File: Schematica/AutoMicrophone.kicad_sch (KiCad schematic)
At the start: 17 parts, among them J1 XLR3_Ground, J2 XLR3_Ground, J3 Jack-DC, Q1 IRLZ44N, Q2 IRLZ44N, Q3 2N3904, U1 SPX2920U-5.0_TO220, U2 ATtiny85-20P

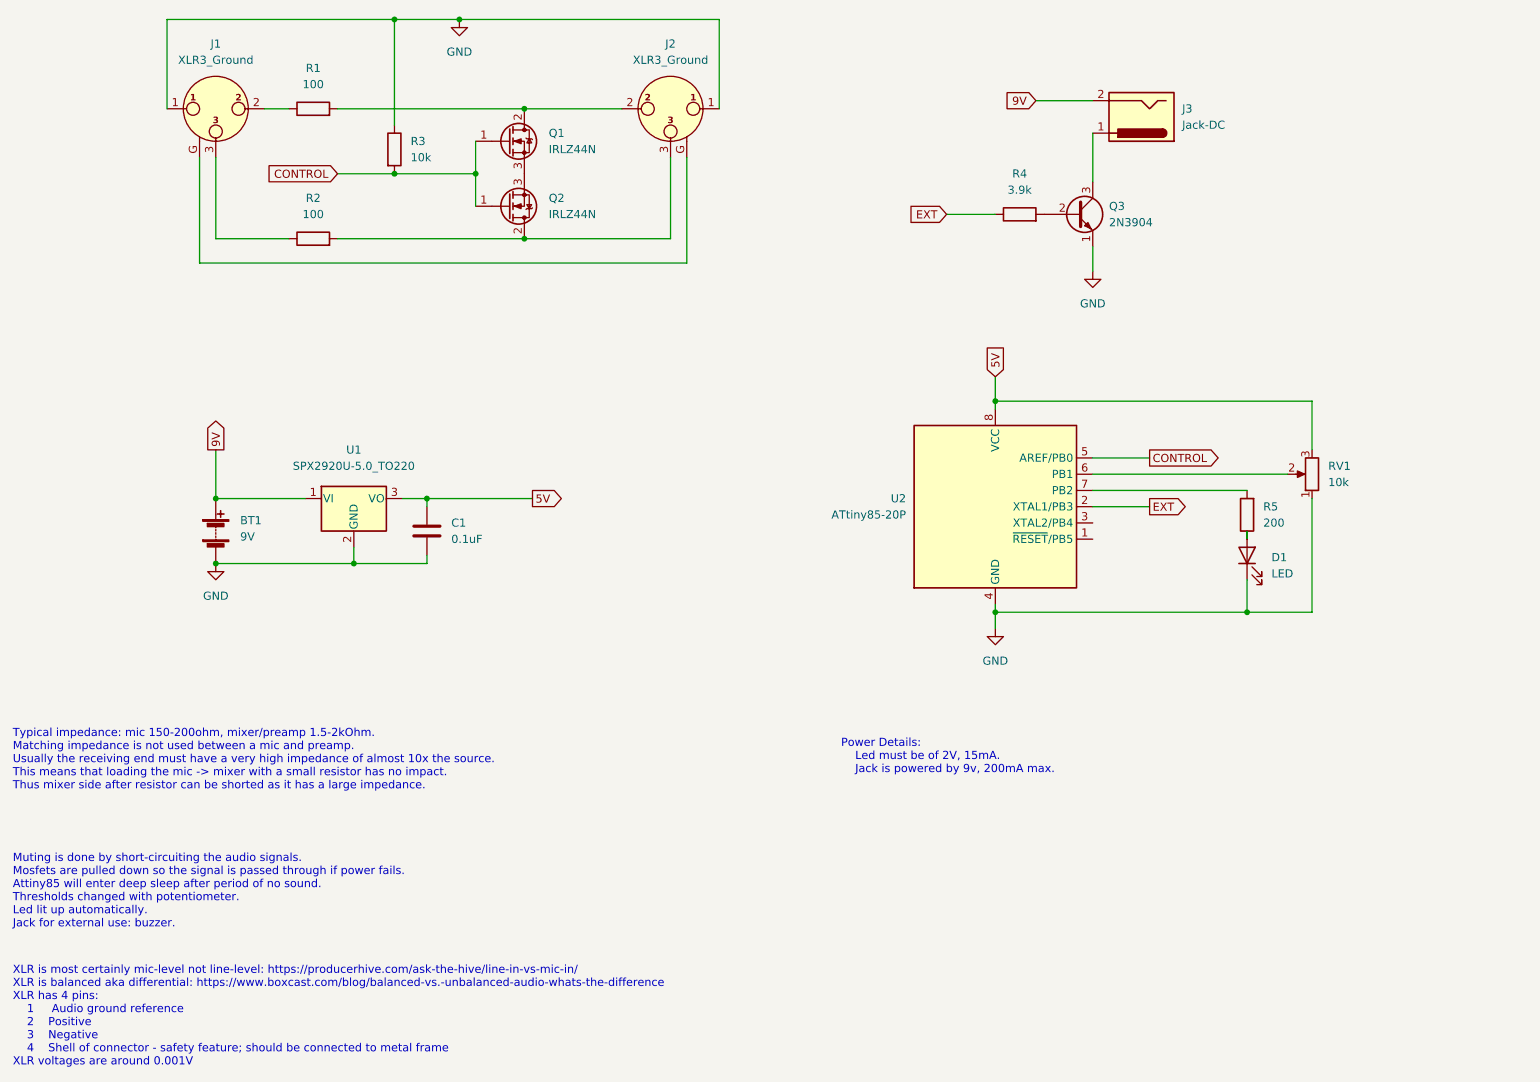
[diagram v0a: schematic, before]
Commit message: Added opamp circuit
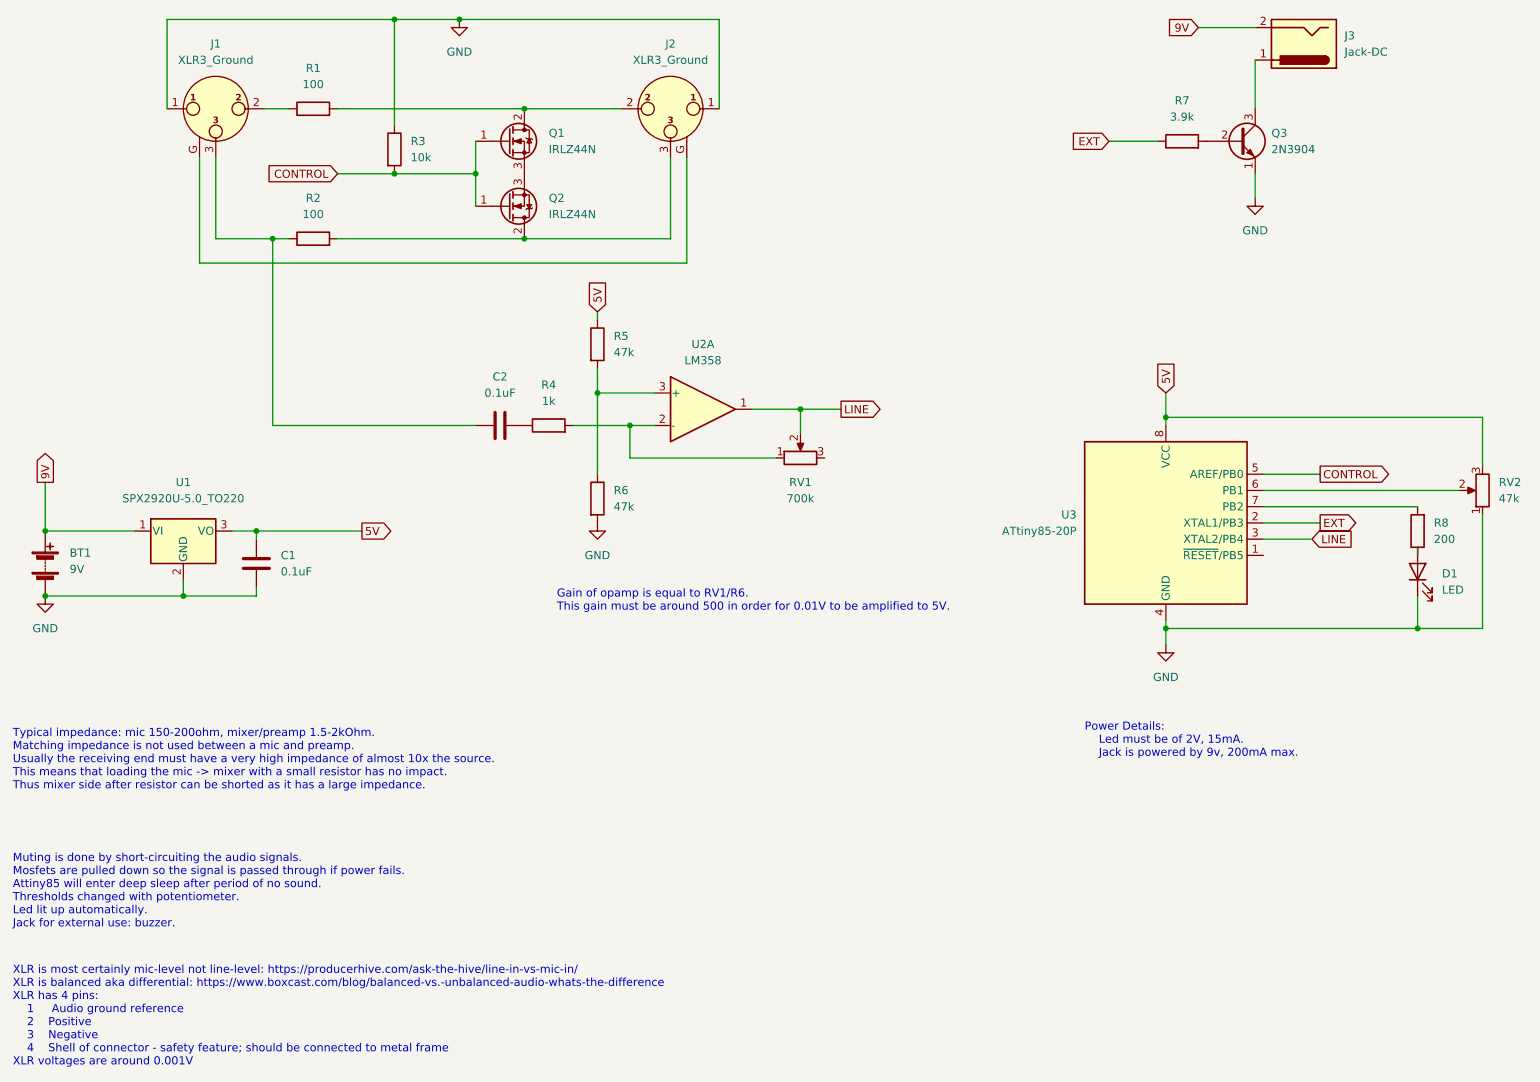
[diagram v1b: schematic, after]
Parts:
- added C2: 0.1uF, symbol Device:C
- added R4: 1k, symbol Device:R
- added R5, R6: 47k, symbol Device:R
- added RV1: 700k, symbol Device:R_Potentiometer
- added U2: LM358, symbol Amplifier_Operational:LM358
- RV2: renamed from RV1; value 10k -> 47k
- renumbered R4 to R7, R5 to R8, U2 to U3
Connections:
- net 5V: now also R5.1
- net GND: now also R6.2
- net at J1.3, R2.1: now also C2.2
- net LINE: now reaches U3.3 (XTAL2/PB4)
- net LINE: now also RV1.2, U2.1
- new net: R4.2, RV1.1, U2.2 (-)
- new net: C2.1, R4.1
- new net: R5.2, R6.1, U2.3 (+)
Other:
- note added: "Gain of opamp is equal to RV1/R6. This gain must be around 500 in order for 0.01V to be amplified to 5V."
- moved on the sheet: BT1, C1, D1, J3, Q3, R7, R8, RV2, U1, U3

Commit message: Update
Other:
- note added: "Gain of opamp is equal to RV1/R4. This gain must be around 500 in order for 0.01V to be amplified to 5V."
- note removed: "Gain of opamp is equal to RV1/R6. This gain must be around 500 in order for 0.01V to be amplified to 5V."
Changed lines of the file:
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@@
     (effects (font (size 1.27 1.27)) (justify left bottom))
   )
-  (text "Gain of opamp is equal to RV1/R6.\nThis gain must be around 500 in order for 0.01V to be amplified to 5V."
+  (text "Gain of opamp is equal to RV1/R4.\nThis gain must be around 500 in order for 0.01V to be amplified to 5V."
     (at 105.41 120.65 0)
     (effects (font (size 1.27 1.27)) (justify left bottom))

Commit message: Update
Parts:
- J1: value XLR3_Ground -> XLR3_Input
- J2: value XLR3_Ground -> XLR3_Output
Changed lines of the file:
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@@
     (in_bom yes) (on_board yes) (fields_autoplaced)
     (property "Reference" "J1" (id 0) (at 52.07 31.75 0))
-    (property "Value" "XLR3_Ground" (id 1) (at 52.07 34.29 0))
+    (property "Value" "XLR3_Input" (id 1) (at 52.07 34.29 0))
     (property "Footprint" "" (id 2) (at 52.07 41.91 0)
       (effects (font (size 1.27 1.27)) hide)
@@
     (in_bom yes) (on_board yes) (fields_autoplaced)
     (property "Reference" "J2" (id 0) (at 123.19 31.75 0))
-    (property "Value" "XLR3_Ground" (id 1) (at 123.19 34.29 0))
+    (property "Value" "XLR3_Output" (id 1) (at 123.19 34.29 0))
     (property "Footprint" "" (id 2) (at 123.19 41.91 0)
       (effects (font (size 1.27 1.27)) hide)
@@
     )
     (path "/517b1f63-2167-4d86-b46b-43a324fbb18c"
-      (reference "J1") (unit 1) (value "XLR3_Ground") (footprint "")
+      (reference "J1") (unit 1) (value "XLR3_Input") (footprint "")
     )
     (path "/a53a6484-d462-4da0-be47-bf38a7498d71"
-      (reference "J2") (unit 1) (value "XLR3_Ground") (footprint "")
+      (reference "J2") (unit 1) (value "XLR3_Output") (footprint "")
     )
     (path "/02d58fd0-76eb-44ff-af71-e2894734b8ee"

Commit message: Removed decoupling capacitor
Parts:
- removed C2: 0.1uF, symbol Device:C
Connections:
- net at R4.1: now also J1.3, R2.1
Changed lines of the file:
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@@
-    (stroke (width 0) (type default) (color 0 0 0 0))
-  )
-  (wire (pts (xy 92.71 91.44) (xy 60.96 91.44))
     (stroke (width 0) (type default) (color 0 0 0 0))
   )
@@
   )
   (wire (pts (xy 60.96 91.44) (xy 60.96 62.23))
+    (stroke (width 0) (type default) (color 0 0 0 0))
+  )
+  (wire (pts (xy 60.96 91.44) (xy 100.33 91.44))
     (stroke (width 0) (type default) (color 0 0 0 0))
   )
@@
     (pin "2")
     (pin "3")
-  )
-  (symbol (lib_id "Device:C") (at 96.52 91.44 270) (unit 1)
-    (in_bom yes) (on_board yes) (fields_autoplaced)
-    (property "Reference" "C2" (id 0) (at 96.52 83.82 90))
-    (property "Value" "0.1uF" (id 1) (at 96.52 86.36 90))
-    (property "Footprint" "" (id 2) (at 92.71 92.4052 0)
-      (effects (font (size 1.27 1.27)) hide)
-    )
-    (property "Datasheet" "~" (id 3) (at 96.52 91.44 0)
-      (effects (font (size 1.27 1.27)) hide)
-    )
-    (pin "1")
-    (pin "2")
   )
   (symbol (lib_id "power:GND") (at 25.4 118.11 0) (unit 1)
@@
       (reference "C1") (unit 1) (value "0.1uF") (footprint "")
     )
-    (path "/3d5742cc-47b6-4f57-a516-2e64d7041236"
-      (reference "C2") (unit 1) (value "0.1uF") (footprint "")
-    )
     (path "/c8230e17-a1ec-4eb2-8d56-74781636f1fa"

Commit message: Update
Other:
- note added: "Gain of opamp is equal to RV1/R4. This gain should be around 500."
- note removed: "Gain of opamp is equal to RV1/R4. This gain must be around 500 in order for 0.01V to be amplified to 5V."
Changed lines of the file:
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@@
     (effects (font (size 1.27 1.27)) (justify left bottom))
   )
-  (text "Gain of opamp is equal to RV1/R4.\nThis gain must be around 500 in order for 0.01V to be amplified to 5V."
+  (text "Gain of opamp is equal to RV1/R4.\nThis gain should be around 500."
     (at 105.41 120.65 0)
     (effects (font (size 1.27 1.27)) (justify left bottom))
